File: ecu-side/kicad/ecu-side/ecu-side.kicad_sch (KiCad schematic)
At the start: 12 parts, among them J1 Conn_01x03, J2 Conn_01x02, U1 ISO7720D, U2 AM26LS31CN, U3 SN74LVC1G17

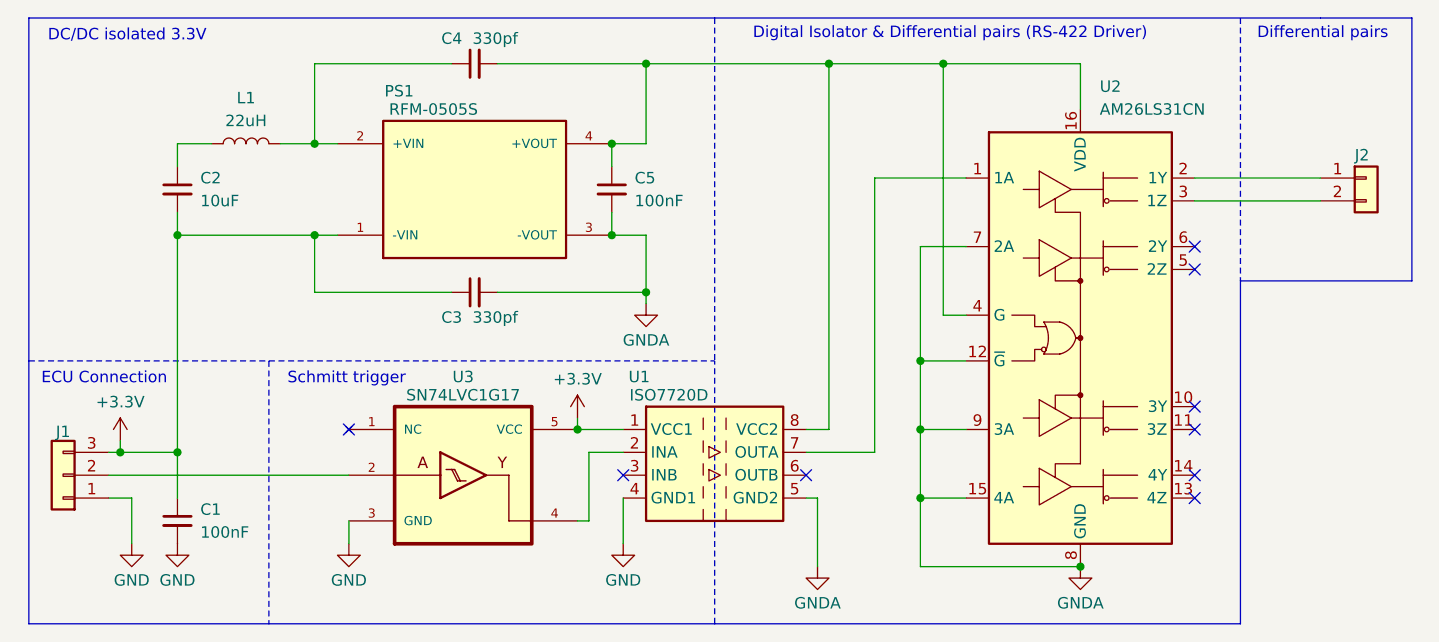
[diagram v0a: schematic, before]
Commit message: corrections tlv9002 replaced with lm458 & ecu 5v domain not 3.3v domain.
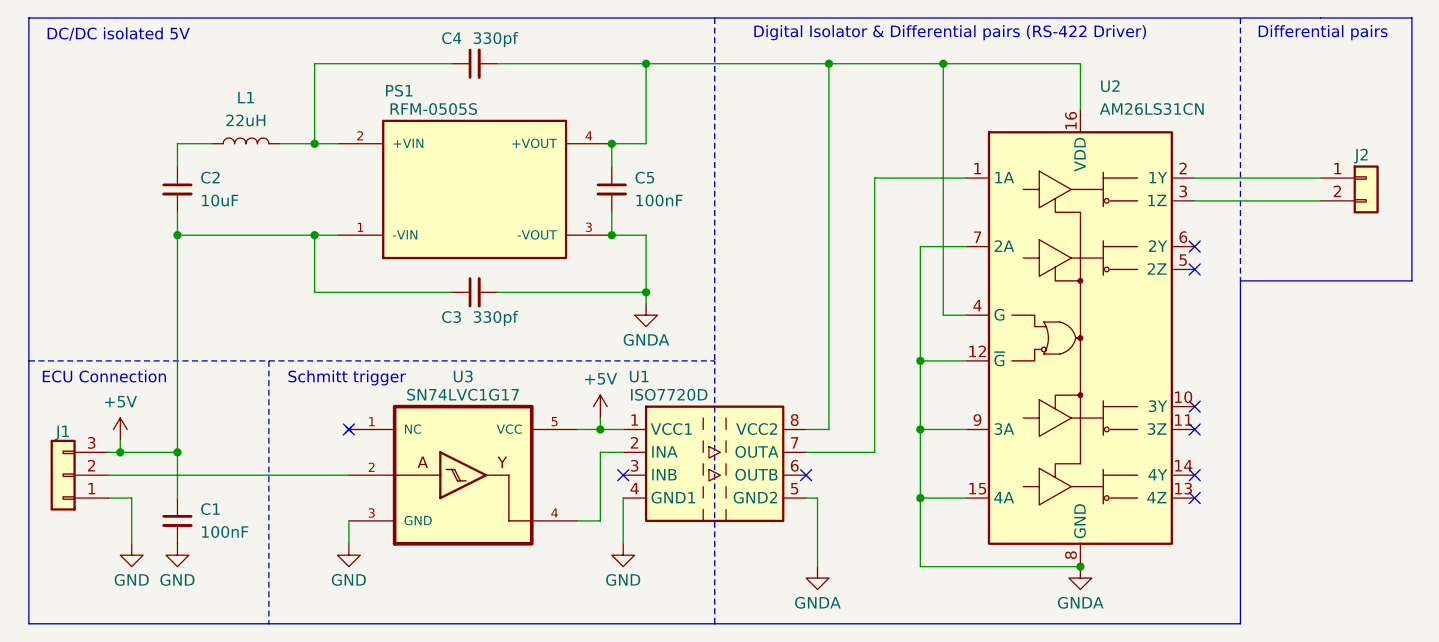
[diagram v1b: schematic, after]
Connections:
- net +3.3V renamed +5V
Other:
- note added: "DC/DC isolated 5V"
- note removed: "DC/DC isolated 3.3V"
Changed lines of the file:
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@@
 		)
 	)
-	(text "DC/DC isolated 3.3V\n"
+	(text "DC/DC isolated 5V\n\n"
 		(exclude_from_sim no)
-		(at 28.702 19.812 0)
+		(at 27.686 20.828 0)
 		(effects
 			(font
@@
 	)
 	(junction
+		(at 81.28 63.5)
+		(diameter 0)
+		(color 0 0 0 0)
+	)
+	(junction
 		(at 34.29 41.91)
 		(diameter 0)
@@
 	)
 	(junction
-		(at 78.74 63.5)
-		(diameter 0)
-		(color 0 0 0 0)
-	)
-	(junction
 		(at 116.84 55.88)
 		(diameter 0)
@@
 	(wire
 		(pts
-			(xy 78.74 63.5) (xy 83.82 63.5)
+			(xy 78.74 63.5) (xy 81.28 63.5)
 		)
 		(stroke
@@
 	(wire
 		(pts
-			(xy 80.01 66.04) (xy 83.82 66.04)
+			(xy 81.28 66.04) (xy 83.82 66.04)
 		)
 		(stroke
@@
 	(wire
 		(pts
-			(xy 78.74 63.5) (xy 78.74 62.23)
-		)
-		(stroke
-			(width 0)
-			(type default)
-		)
-	)
-	(wire
-		(pts
-			(xy 80.01 73.66) (xy 80.01 66.04)
+			(xy 81.28 73.66) (xy 81.28 66.04)
 		)
 		(stroke
@@
 	(wire
 		(pts
-			(xy 80.01 73.66) (xy 78.74 73.66)
+			(xy 81.28 73.66) (xy 78.74 73.66)
 		)
 		(stroke
@@
 	(wire
 		(pts
+			(xy 81.28 63.5) (xy 83.82 63.5)
+		)
+		(stroke
+			(width 0)
+			(type default)
+		)
+	)
+	(wire
+		(pts
 			(xy 147.32 35.56) (xy 161.29 35.56)
 		)
@@
 		(pts
 			(xy 34.29 39.37) (xy 34.29 41.91)
+		)
+		(stroke
+			(width 0)
+			(type default)
+		)
+	)
+	(wire
+		(pts
+			(xy 81.28 62.23) (xy 81.28 63.5)
 		)
 		(stroke
@@
 			)
 		)
-		(property "Value" "+3.3V"
+		(property "Value" "+5V"
 			(at 27.94 60.452 0)
 			(show_name no)
@@
 	)
 	(symbol
-		(lib_id "power:+3.3V")
-		(at 78.74 62.23 0)
-		(unit 1)
-		(body_style 1)
-		(exclude_from_sim no)
-		(in_bom yes)
-		(on_board yes)
-		(in_pos_files yes)
-		(dnp no)
-		(property "Reference" "#PWR09"
-			(at 78.74 66.04 0)
-			(hide yes)
-			(show_name no)
-			(do_not_autoplace no)
-			(effects
-				(font
-					(size 1.27 1.27)
-				)
-			)
-		)
-		(property "Value" "+3.3V"
-			(at 78.74 57.912 0)
-			(show_name no)
-			(do_not_autoplace no)
-			(effects
-				(font
-					(size 1.27 1.27)
-				)
-			)
-		)
-		(property "Footprint" ""
-			(at 78.74 62.23 0)
-			(hide yes)
-			(show_name no)
-			(do_not_autoplace no)
-			(effects
-				(font
-					(size 1.27 1.27)
-				)
-			)
-		)
-		(property "Datasheet" ""
-			(at 78.74 62.23 0)
-			(hide yes)
-			(show_name no)
-			(do_not_autoplace no)
-			(effects
-				(font
-					(size 1.27 1.27)
-				)
-			)
-		)
-		(property "Description" "Power symbol creates a global label with name \"+3.3V\""
-			(at 78.74 62.23 0)
-			(hide yes)
-			(show_name no)
-			(do_not_autoplace no)
-			(effects
-				(font
-					(size 1.27 1.27)
-				)
-			)
-		)
-		(pin "1"
-		)
-		(instances
-			(project "ecu-side"
-				(path "/44fd82d1-1a19-4a10-963a-e6547fd44ac6"
-					(reference "#PWR09")
-					(unit 1)
-				)
-			)
-		)
-	)
-	(symbol
 		(lib_id "RFM-0505S:RFM-0505S")
 		(at 67.31 36.83 0)
@@
 					(unit 1)
 				)
+			)
+		)
+	)
+	(symbol
+		(lib_id "power:+3.3V")
+		(at 81.28 62.23 0)
+		(unit 1)
+		(body_style 1)
+		(exclude_from_sim no)
+		(in_bom yes)
+		(on_board yes)
+		(in_pos_files yes)
+		(dnp no)
+		(property "Reference" "#PWR08"
+			(at 81.28 66.04 0)
+			(hide yes)
+			(show_name no)
+			(do_not_autoplace no)
+			(effects
+				(font
+					(size 1.27 1.27)
+				)
+			)
+		)
+		(property "Value" "+5V"
+			(at 81.28 57.912 0)
+			(show_name no)
+			(do_not_autoplace no)
+			(effects
+				(font
+					(size 1.27 1.27)
+				)
+			)
+		)
+		(property "Footprint" ""
+			(at 81.28 62.23 0)
+			(hide yes)
+			(show_name no)
+			(do_not_autoplace no)
+			(effects
+				(font
+					(size 1.27 1.27)
+				)
+			)
+		)
+		(property "Datasheet" ""
+			(at 81.28 62.23 0)
+			(hide yes)
+			(show_name no)
+			(do_not_autoplace no)
+			(effects
+				(font
+					(size 1.27 1.27)
+				)
+			)
+		)
+		(property "Description" "Power symbol creates a global label with name \"+3.3V\""
+			(at 81.28 62.23 0)
+			(hide yes)
+			(show_name no)
+			(do_not_autoplace no)
+			(effects
+				(font
+					(size 1.27 1.27)
+				)
+			)
+		)
+		(pin "1"
+		)
+		(instances
+			(project "ecu-side"
+				(path "/44fd82d1-1a19-4a10-963a-e6547fd44ac6"
+					(reference "#PWR08")
+					(unit 1)
+				)
